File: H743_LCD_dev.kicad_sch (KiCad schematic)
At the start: 4 parts

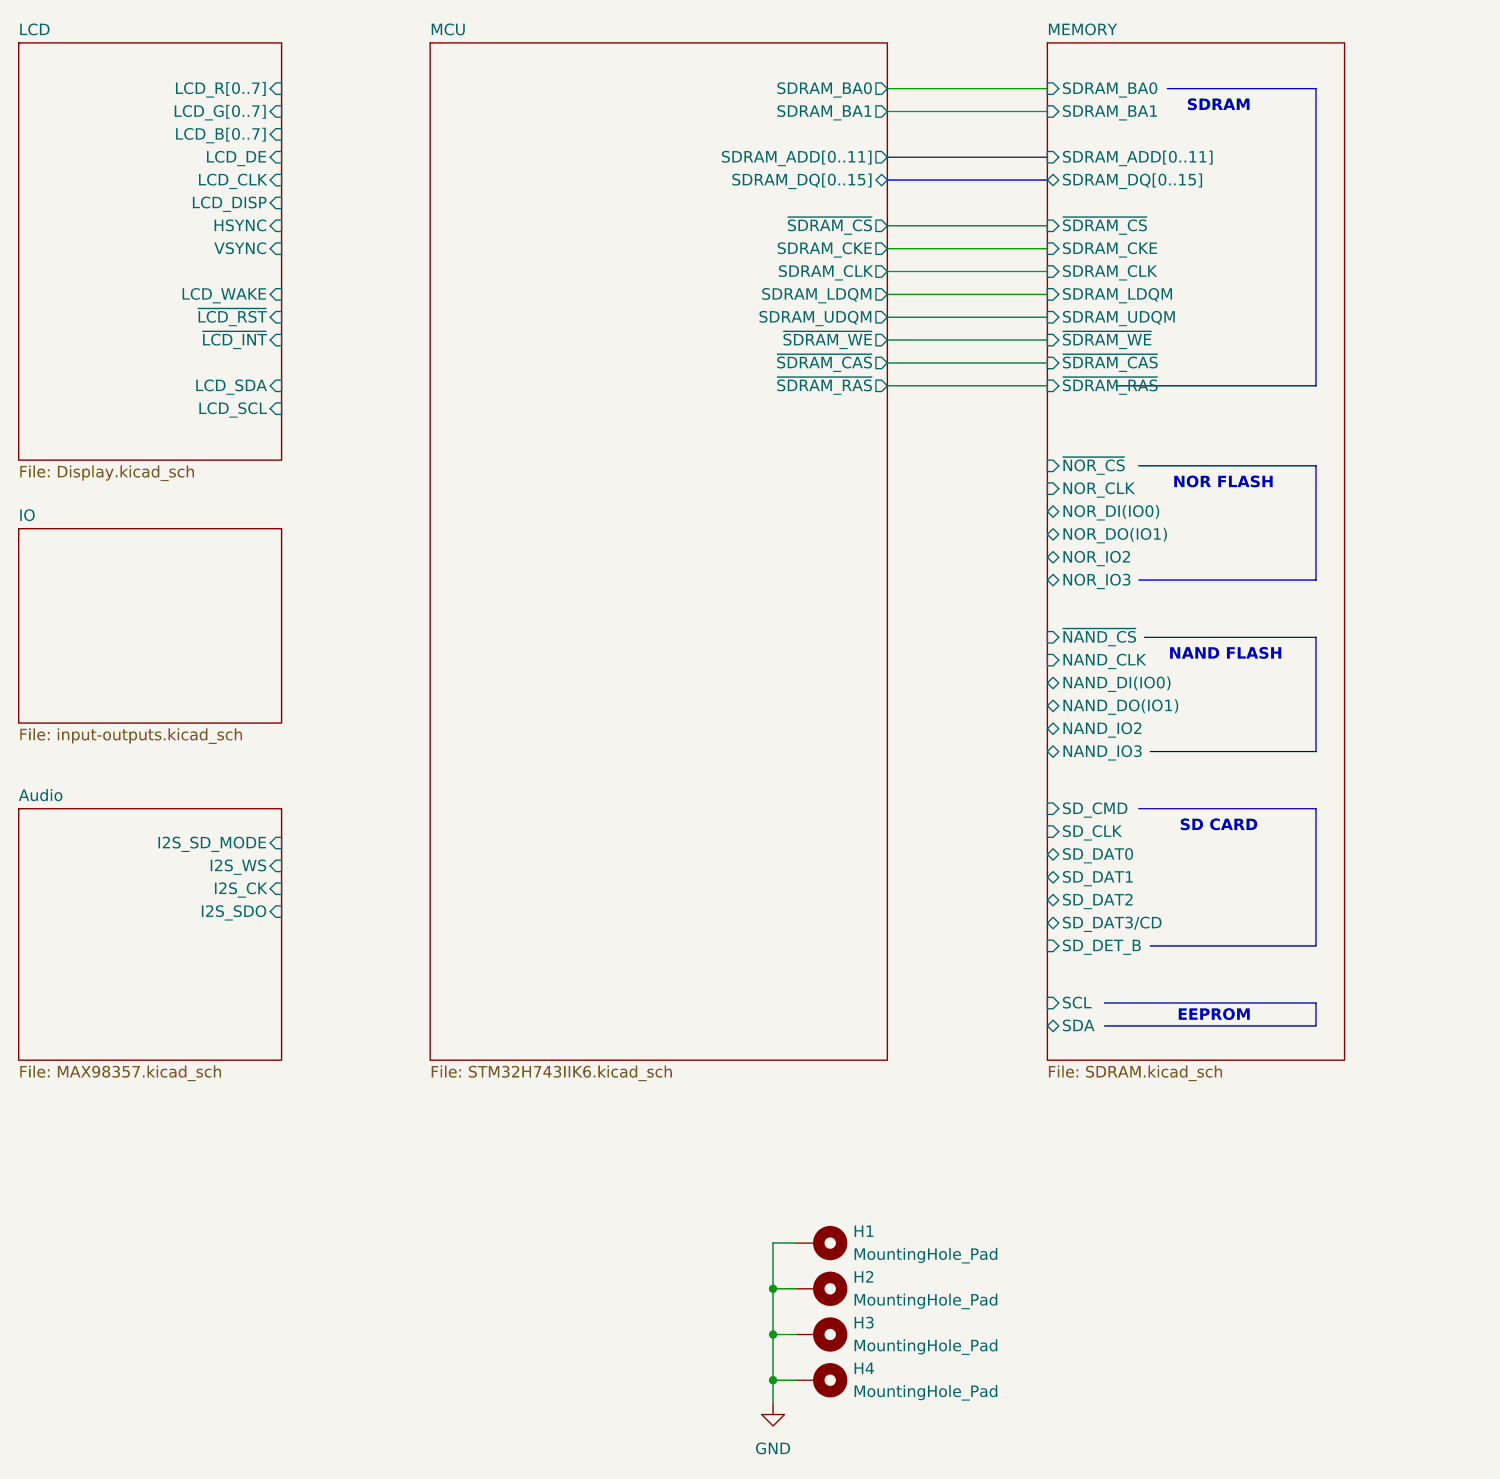
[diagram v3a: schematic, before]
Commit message: Finish sdram, LCD, SD-card, QSPI, I2S tracks
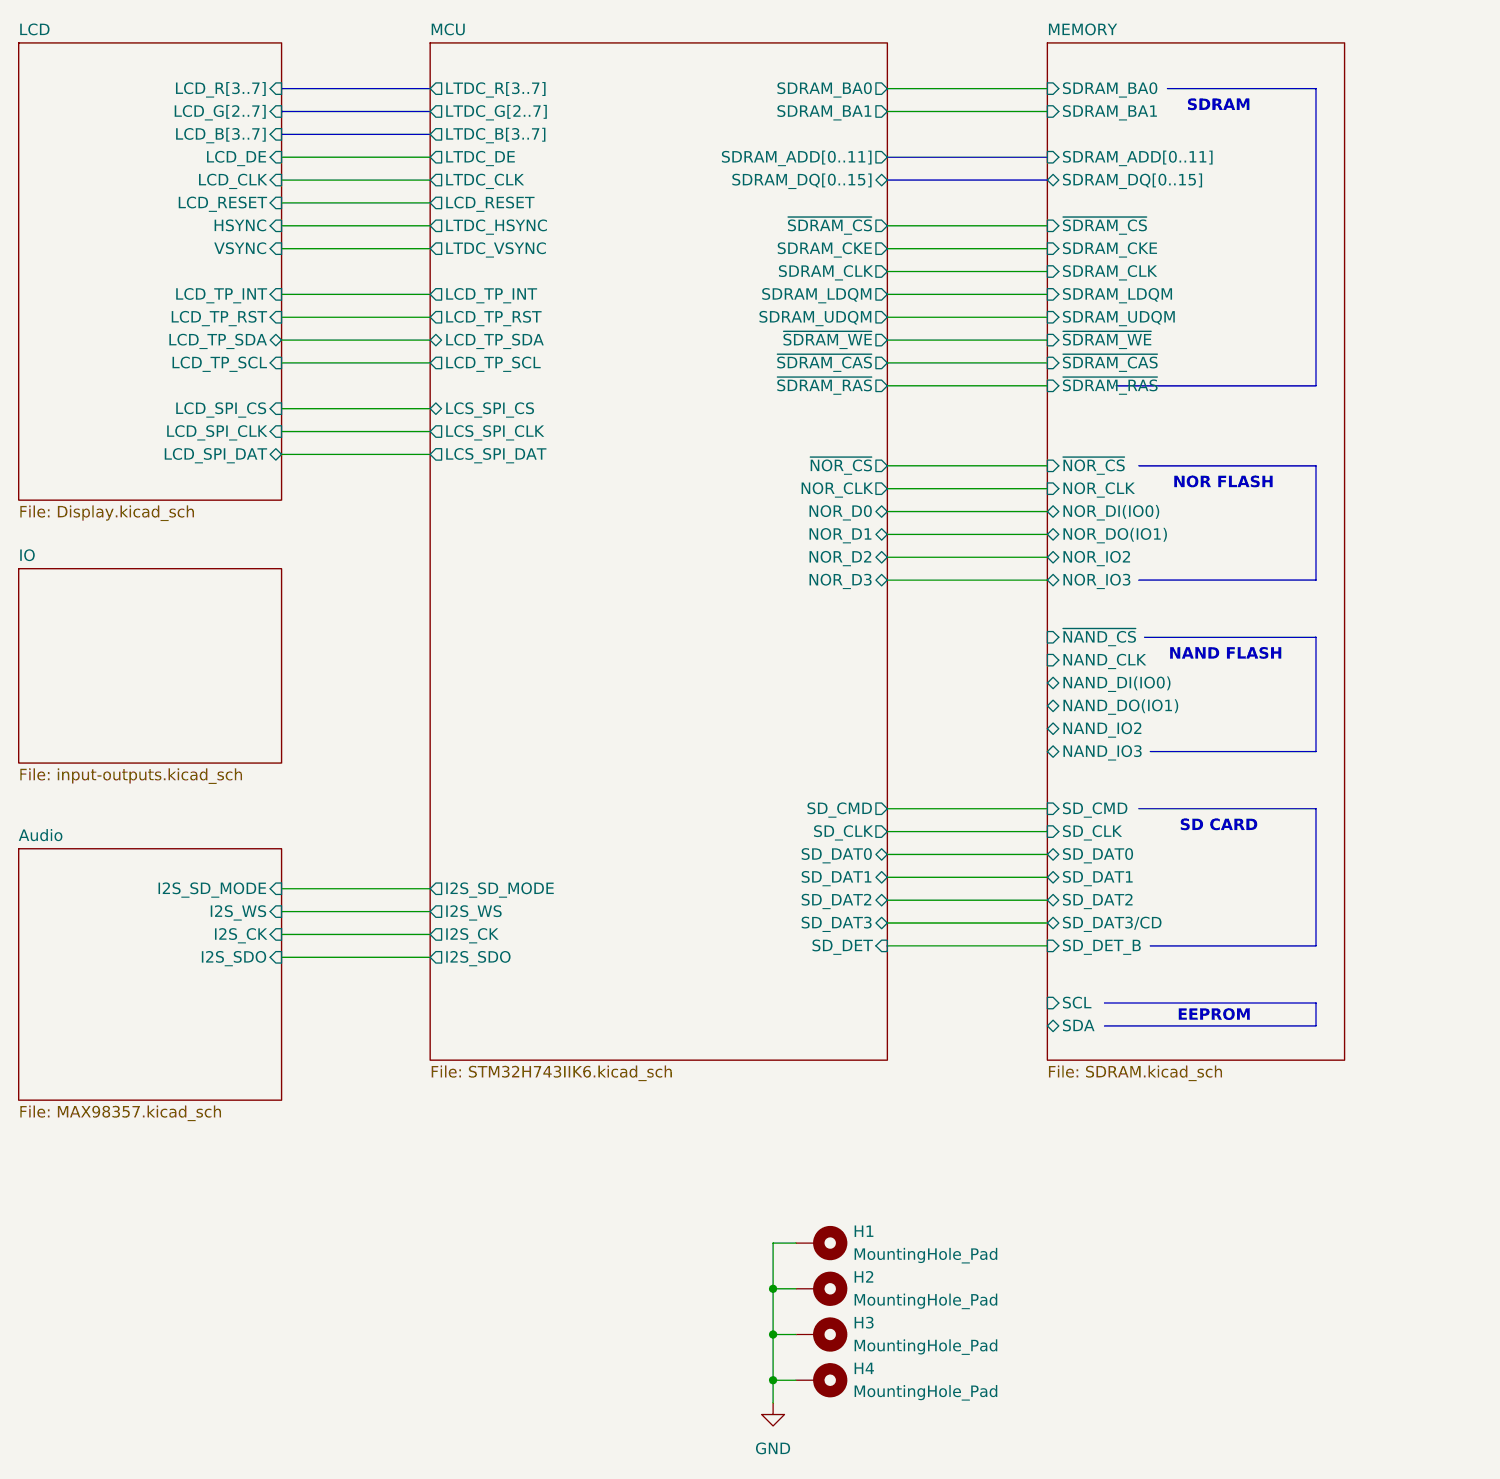
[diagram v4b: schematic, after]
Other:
- sheet LCD ports: added LCD_B[3..7], LCD_G[2..7], LCD_RESET, LCD_R[3..7], LCD_SPI_CLK, LCD_SPI_CS, LCD_SPI_DAT, LCD_TP_INT, LCD_TP_RST, LCD_TP_SCL, LCD_TP_SDA; removed LCD_B[0..7], LCD_DISP, LCD_G[0..7], LCD_R[0..7], LCD_SCL, LCD_SDA, LCD_WAKE, ~{LCD_INT}, ~{LCD_RST}
- sheet MCU ports: added I2S_CK, I2S_SDO, I2S_SD_MODE, I2S_WS, LCD_RESET, LCD_TP_INT, LCD_TP_RST, LCD_TP_SCL, LCD_TP_SDA, LCS_SPI_CLK, LCS_SPI_CS, LCS_SPI_DAT, LTDC_B[3..7], LTDC_CLK, LTDC_DE, LTDC_G[2..7], LTDC_HSYNC, LTDC_R[3..7], LTDC_VSYNC, NOR_CLK, NOR_D0, NOR_D1, NOR_D2, NOR_D3, SD_CLK, SD_CMD, SD_DAT0, SD_DAT1, SD_DAT2, SD_DAT3, SD_DET, ~{NOR_CS}; removed none

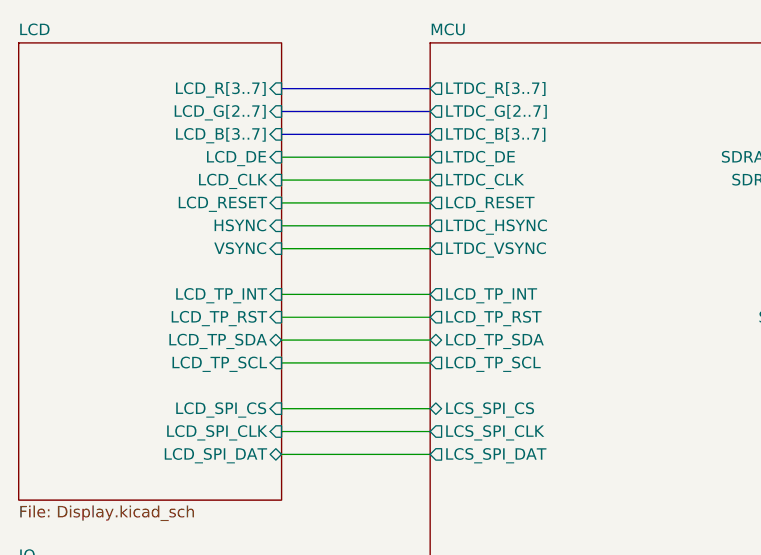
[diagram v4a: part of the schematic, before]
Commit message: Looks like FPC should be changed to XF2M-4015-1A
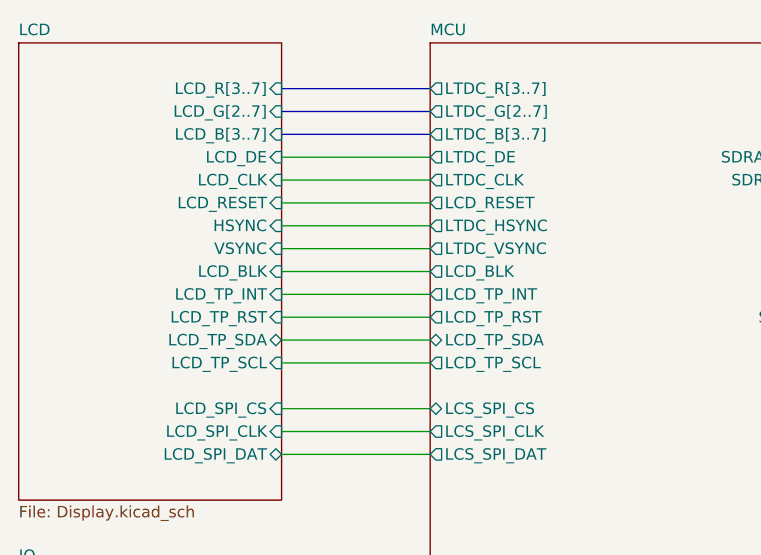
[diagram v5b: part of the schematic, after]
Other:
- sheet LCD ports: added LCD_BLK; removed none
- sheet MCU ports: added LCD_BLK; removed none
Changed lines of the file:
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@@
+	(wire
+		(pts
+			(xy 87.63 52.07) (xy 104.14 52.07)
+		)
+		(stroke
+			(width 0)
+			(type default)
+		)
+	)
 	(wire
 		(pts
@@
 			)
 		)
+		(property "JLCPCB Part #" ""
+			(at 147.32 170.18 0)
+			(effects
+				(font
+					(size 1.27 1.27)
+				)
+				(hide yes)
+			)
+		)
 		(pin "1"
 		)
@@
 			)
 		)
+		(property "JLCPCB Part #" ""
+			(at 147.32 175.26 0)
+			(effects
+				(font
+					(size 1.27 1.27)
+				)
+				(hide yes)
+			)
+		)
 		(pin "1"
 		)
@@
 			)
 		)
+		(property "JLCPCB Part #" ""
+			(at 147.32 165.1 0)
+			(effects
+				(font
+					(size 1.27 1.27)
+				)
+				(hide yes)
+			)
+		)
 		(pin "1"
 		)
@@
 			)
 		)
+		(property "JLCPCB Part #" ""
+			(at 147.32 160.02 0)
+			(effects
+				(font
+					(size 1.27 1.27)
+				)
+				(hide yes)
+			)
+		)
 		(pin "1"
 		)
@@
 			)
 		)
+		(pin "LCD_BLK" output
+			(at 104.14 52.07 180)
+			(effects
+				(font
+					(size 1.27 1.27)
+				)
+				(justify left)
+			)
+		)
 		(instances
 			(project "H743_LCD_dev"
@@
 			(effects
 				(font
+					(size 1.27 1.27)
+				)
+				(justify right)
+			)
+		)
+		(pin "LCD_BLK" input
+			(at 87.63 52.07 0)
+			(effects
+				(font

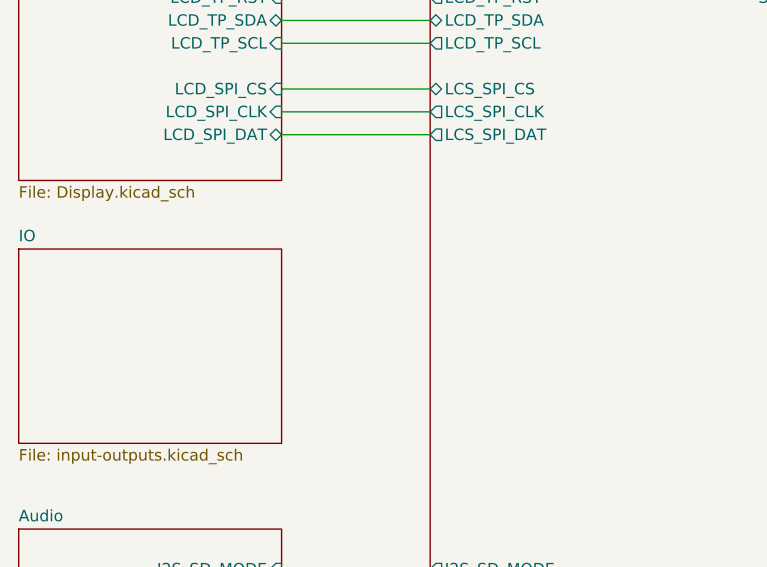
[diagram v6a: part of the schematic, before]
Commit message: Added UART esd
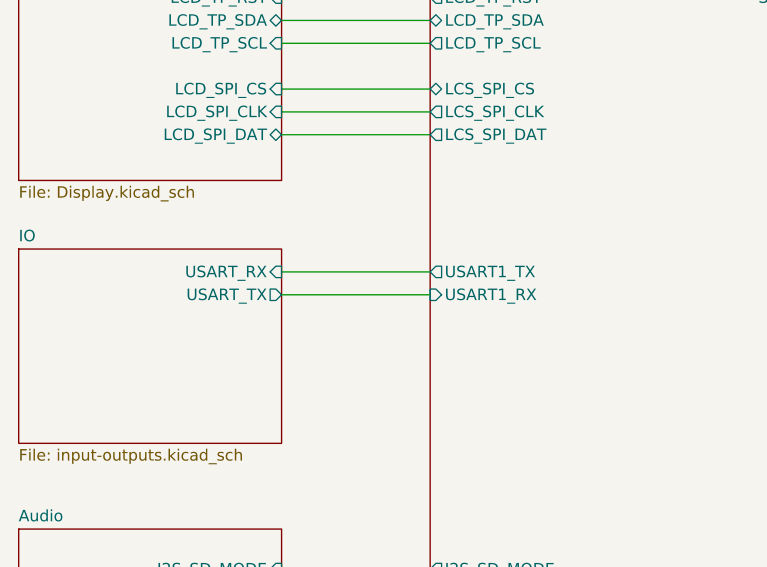
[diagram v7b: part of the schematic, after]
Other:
- sheet IO ports: added USART_RX, USART_TX; removed none
- sheet MCU ports: added USART1_RX, USART1_TX; removed none
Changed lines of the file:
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@@
+	(wire
+		(pts
+			(xy 87.63 90.17) (xy 104.14 90.17)
+		)
+		(stroke
+			(width 0)
+			(type default)
+		)
+	)
 	(wire
 		(pts
@@
 		(pts
 			(xy 154.94 121.92) (xy 172.72 121.92)
+		)
+		(stroke
+			(width 0)
+			(type default)
+		)
+	)
+	(wire
+		(pts
+			(xy 87.63 87.63) (xy 104.14 87.63)
 		)
 		(stroke
@@
 			)
 		)
+		(pin "USART1_TX" output
+			(at 104.14 87.63 180)
+			(effects
+				(font
+					(size 1.27 1.27)
+				)
+				(justify left)
+			)
+		)
+		(pin "USART1_RX" input
+			(at 104.14 90.17 180)
+			(effects
+				(font
+					(size 1.27 1.27)
+				)
+				(justify left)
+			)
+		)
 		(instances
 			(project "H743_LCD_dev"
@@
 			)
 		)
+		(pin "USART_RX" input
+			(at 87.63 87.63 0)
+			(effects
+				(font
+					(size 1.27 1.27)
+				)
+				(justify right)
+			)
+		)
+		(pin "USART_TX" output
+			(at 87.63 90.17 0)
+			(effects
+				(font
+					(size 1.27 1.27)
+				)
+				(justify right)
+			)
+		)
